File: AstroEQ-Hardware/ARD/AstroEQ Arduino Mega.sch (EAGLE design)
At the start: 18 parts, among them J1 POWER_JACKPTH, M0 Motor Driver, M1 Motor Driver

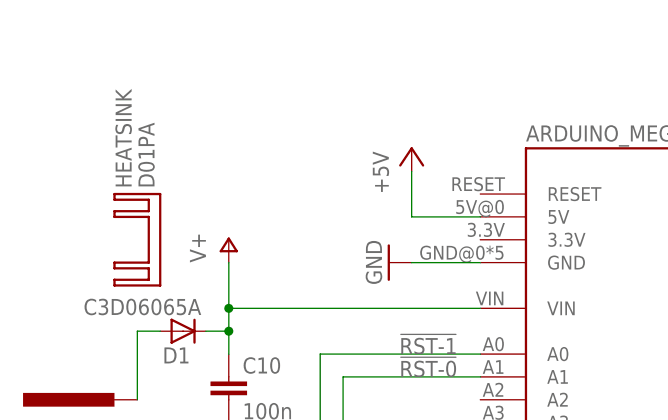
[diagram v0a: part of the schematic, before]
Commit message: Update PCB Logo
Add AstroEQ logo to PCB hardware designs.
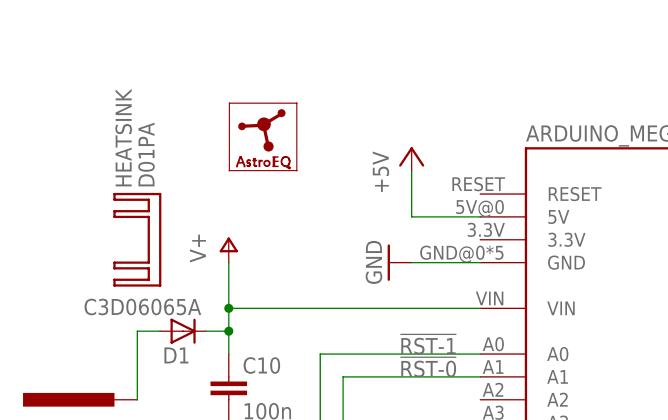
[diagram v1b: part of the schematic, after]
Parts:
- added LOGO1: ASTROEQ8MM, CompanyLogos:ASTROEQ8MM
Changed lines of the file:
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@@
 <grid distance="0.1" unitdist="inch" unit="inch" style="lines" multiple="1" display="no" altdistance="0.01" altunitdist="inch" altunit="inch"/>
 <layers>
-<layer number="1" name="Top" color="4" fill="1" visible="no" active="no"/>
-<layer number="2" name="Route2" color="1" fill="3" visible="no" active="no"/>
-<layer number="3" name="Route3" color="4" fill="3" visible="no" active="no"/>
-<layer number="14" name="Route14" color="1" fill="6" visible="no" active="no"/>
-<layer number="15" name="Route15" color="4" fill="6" visible="no" active="no"/>
-<layer number="16" name="Bottom" color="1" fill="1" visible="no" active="no"/>
-<layer number="17" name="Pads" color="2" fill="1" visible="no" active="no"/>
-<layer number="18" name="Vias" color="2" fill="1" visible="no" active="no"/>
-<layer number="19" name="Unrouted" color="6" fill="1" visible="no" active="no"/>
-<layer number="20" name="Dimension" color="15" fill="1" visible="no" active="no"/>
-<layer number="21" name="tPlace" color="7" fill="1" visible="no" active="no"/>
-<layer number="22" name="bPlace" color="7" fill="1" visible="no" active="no"/>
-<layer number="23" name="tOrigins" color="15" fill="1" visible="no" active="no"/>
-<layer number="24" name="bOrigins" color="15" fill="1" visible="no" active="no"/>
-<layer number="25" name="tNames" color="15" fill="1" visible="no" active="no"/>
-<layer number="26" name="bNames" color="7" fill="1" visible="no" active="no"/>
-<layer number="27" name="tValues" color="15" fill="1" visible="no" active="no"/>
-<layer number="28" name="bValues" color="7" fill="1" visible="no" active="no"/>
+<layer number="1" name="Top" color="4" fill="1" visible="yes" active="no"/>
+<layer number="2" name="Route2" color="1" fill="3" visible="yes" active="no"/>
+<layer number="3" name="Route3" color="4" fill="3" visible="yes" active="no"/>
+<layer number="14" name="Route14" color="1" fill="6" visible="yes" active="no"/>
+<layer number="15" name="Route15" color="4" fill="6" visible="yes" active="no"/>
+<layer number="16" name="Bottom" color="1" fill="1" visible="yes" active="no"/>
+<layer number="17" name="Pads" color="2" fill="1" visible="yes" active="no"/>
+<layer number="18" name="Vias" color="2" fill="1" visible="yes" active="no"/>
+<layer number="19" name="Unrouted" color="6" fill="1" visible="yes" active="no"/>
+<layer number="20" name="Dimension" color="15" fill="1" visible="yes" active="no"/>
+<layer number="21" name="tPlace" color="7" fill="1" visible="yes" active="no"/>
+<layer number="22" name="bPlace" color="7" fill="1" visible="yes" active="no"/>
+<layer number="23" name="tOrigins" color="15" fill="1" visible="yes" active="no"/>
+<layer number="24" name="bOrigins" color="15" fill="1" visible="yes" active="no"/>
+<layer number="25" name="tNames" color="15" fill="1" visible="yes" active="no"/>
+<layer number="26" name="bNames" color="7" fill="1" visible="yes" active="no"/>
+<layer number="27" name="tValues" color="15" fill="1" visible="yes" active="no"/>
+<layer number="28" name="bValues" color="7" fill="1" visible="yes" active="no"/>
 <layer number="29" name="tStop" color="7" fill="3" visible="no" active="no"/>
 <layer number="30" name="bStop" color="7" fill="6" visible="no" active="no"/>
@@
 <layer number="35" name="tGlue" color="7" fill="4" visible="no" active="no"/>
 <layer number="36" name="bGlue" color="7" fill="5" visible="no" active="no"/>
-<layer number="37" name="tTest" color="7" fill="1" visible="no" active="no"/>
-<layer number="38" name="bTest" color="7" fill="1" visible="no" active="no"/>
+<layer number="37" name="tTest" color="7" fill="1" visible="yes" active="no"/>
+<layer number="38" name="bTest" color="7" fill="1" visible="yes" active="no"/>
 <layer number="39" name="tKeepout" color="4" fill="11" visible="no" active="no"/>
 <layer number="40" name="bKeepout" color="1" fill="11" visible="no" active="no"/>
@@
 <layer number="44" name="Drills" color="15" fill="1" visible="no" active="no"/>
 <layer number="45" name="Holes" color="15" fill="1" visible="no" active="no"/>
-<layer number="46" name="Milling" color="3" fill="1" visible="no" active="no"/>
-<layer number="47" name="Measures" color="7" fill="1" visible="no" active="no"/>
-<layer number="48" name="Document" color="7" fill="1" visible="no" active="no"/>
-<layer number="49" name="Reference" color="7" fill="1" visible="no" active="no"/>
-<layer number="50" name="dxf" color="7" fill="1" visible="no" active="no"/>
-<layer number="51" name="tDocu" color="7" fill="1" visible="no" active="no"/>
-<layer number="52" name="bDocu" color="7" fill="1" visible="no" active="no"/>
-<layer number="53" name="tGND_GNDA" color="7" fill="9" visible="no" active="no"/>
-<layer number="54" name="bGND_GNDA" color="1" fill="9" visible="no" active="no"/>
-<layer number="56" name="wert" color="7" fill="1" visible="no" active="no"/>
+<layer number="46" name="Milling" color="3" fill="1" visible="yes" active="no"/>
+<layer number="47" name="Measures" color="7" fill="1" visible="yes" active="no"/>
+<layer number="48" name="Document" color="7" fill="1" visible="yes" active="no"/>
+<layer number="49" name="Reference" color="7" fill="1" visible="yes" active="no"/>
+<layer number="50" name="dxf" color="7" fill="1" visible="yes" active="no"/>
+<layer number="51" name="tDocu" color="7" fill="1" visible="yes" active="no"/>
+<layer number="52" name="bDocu" color="7" fill="1" visible="yes" active="no"/>
+<layer number="53" name="tGND_GNDA" color="7" fill="9" visible="yes" active="no"/>
+<layer number="54" name="bGND_GNDA" color="1" fill="9" visible="yes" active="no"/>
+<layer number="56" name="wert" color="7" fill="1" visible="yes" active="no"/>
 <layer number="91" name="Nets" color="2" fill="1" visible="yes" active="yes"/>
 <layer number="92" name="Busses" color="1" fill="1" visible="yes" active="yes"/>
@@
 <layer number="110" name="fp0" color="7" fill="1" visible="no" active="yes"/>
 <layer number="111" name="LPC17xx" color="7" fill="1" visible="yes" active="yes"/>
+<layer number="112" name="tSilk" color="7" fill="1" visible="no" active="yes"/>
 <layer number="116" name="Patch_BOT" color="9" fill="4" visible="no" active="yes"/>
 <layer number="121" name="_tsilk" color="7" fill="1" visible="no" active="yes"/>
@@
 <layer number="124" name="bTestmark" color="7" fill="1" visible="no" active="yes"/>
 <layer number="125" name="_tNames" color="7" fill="1" visible="no" active="yes"/>
+<layer number="126" name="_bNames" color="7" fill="1" visible="no" active="yes"/>
+<layer number="127" name="_tValues" color="7" fill="1" visible="no" active="yes"/>
+<layer number="128" name="_bValues" color="7" fill="1" visible="no" active="yes"/>
 <layer number="131" name="tAdjust" color="7" fill="1" visible="no" active="yes"/>
 <layer number="132" name="bAdjust" color="7" fill="1" visible="no" active="yes"/>
 <layer number="144" name="Drill_legend" color="7" fill="1" visible="no" active="yes"/>
 <layer number="151" name="HeatSink" color="7" fill="1" visible="no" active="yes"/>
+<layer number="152" name="_bDocu" color="7" fill="1" visible="no" active="yes"/>
 <layer number="199" name="Contour" color="7" fill="1" visible="yes" active="yes"/>
 <layer number="200" name="200bmp" color="1" fill="10" visible="no" active="yes"/>
@@
 <layer number="223" name="223bmp" color="24" fill="1" visible="no" active="no"/>
 <layer number="224" name="224bmp" color="25" fill="1" visible="no" active="no"/>
+<layer number="248" name="Housing" color="7" fill="1" visible="no" active="yes"/>
+<layer number="249" name="Edge" color="7" fill="1" visible="no" active="yes"/>
 <layer number="250" name="Descript" color="3" fill="1" visible="no" active="no"/>
 <layer number="251" name="SMDround" color="12" fill="11" visible="no" active="no"/>
@@
 <part name="HEATSINK" library="heatsink" deviceset="D01PA" device=""/>
 <part name="P+3" library="supply1" deviceset="V+" device=""/>
+<part name="LOGO1" library="CompanyLogos" deviceset="ASTROEQ" device="8MM" value="ASTROEQ8MM"/>
 </parts>
 <sheets>
@@
 <instance part="HEATSINK" gate="G$1" x="20.32" y="111.76" rot="R90"/>
 <instance part="P+3" gate="1" x="129.54" y="134.62"/>
+<instance part="LOGO1" gate="G$1" x="27.94" y="119.38"/>
 </instances>
 <busses>

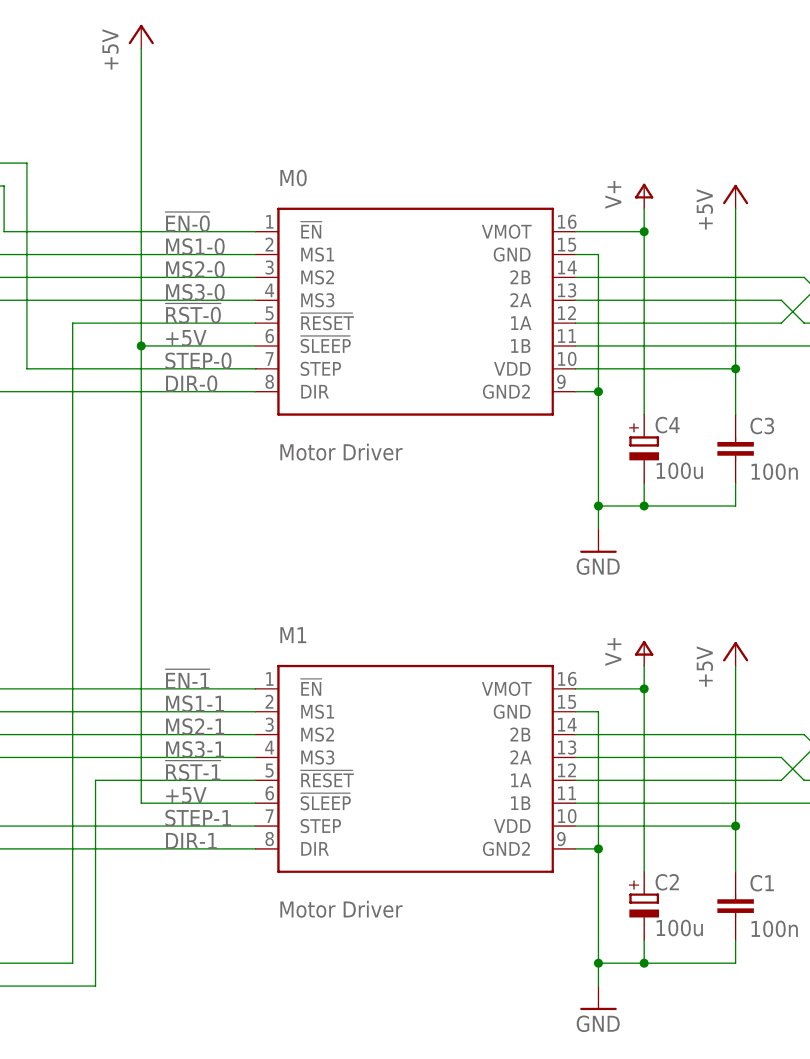
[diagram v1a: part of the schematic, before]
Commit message: Correct Schematic Labelling
Correct labelling in schematic and add additional information to avoid confusion with pin assignments on driver boards.
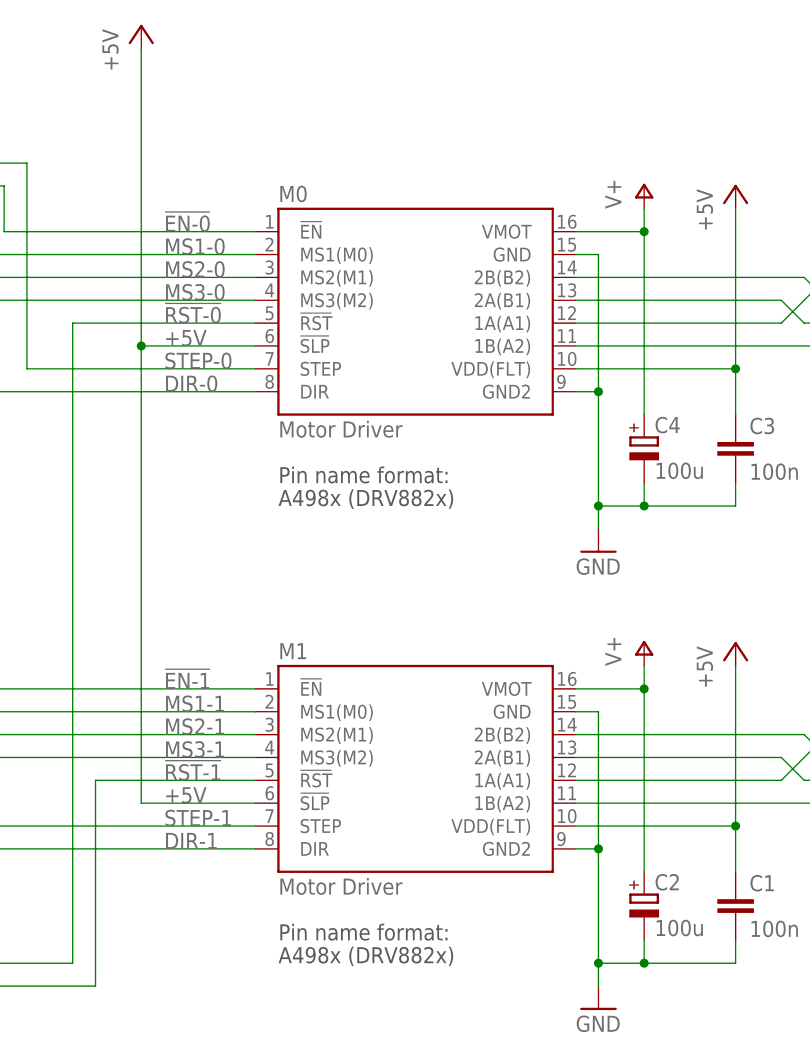
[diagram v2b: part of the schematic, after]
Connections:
- net !RST-0: now also M0.!RST; no longer M0.!RESET
- net !RST-1: now also M1.!RST; no longer M1.!RESET
- net +5V: now also M0.!SLP, M0.VDD(FLT), M1.!SLP, M1.VDD(FLT); no longer M0.!SLEEP, M0.VDD, M1.!SLEEP, M1.VDD
- net DEC-1A: now also M1.1A(A1); no longer M1.1A
- net DEC-1B: now also M1.1B(A2); no longer M1.1B
- net DEC-2A: now also M1.2A(B1); no longer M1.2A
- net DEC-2B: now also M1.2B(B2); no longer M1.2B
- net MS1-0: now also M0.MS1(M0); no longer M0.MS1
- net MS1-1: now also M1.MS1(M0); no longer M1.MS1
- net MS2-0: now also M0.MS2(M1); no longer M0.MS2
- net MS2-1: now also M1.MS2(M1); no longer M1.MS2
- net MS3-0: now also M0.MS3(M2); no longer M0.MS3
- net MS3-1: now also M1.MS3(M2); no longer M1.MS3
- net RA-1A: now also M0.1A(A1); no longer M0.1A
- net RA-1B: now also M0.1B(A2); no longer M0.1B
- net RA-2A: now also M0.2A(B1); no longer M0.2A
- net RA-2B: now also M0.2B(B2); no longer M0.2B
